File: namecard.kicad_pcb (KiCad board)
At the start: 2 copper layers, 85.6 x 54 mm, 29 parts, among them J1 Conn_01x24, J2 Conn_01x05, Q1 AO3400A, U1 STM32G030K6Tx, U2 ST25DV04K-IER8C3

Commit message: 基盤配置の調整
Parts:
- removed C_Tank1: 330uF, Capacitor_Tantalum_SMD:CP_EIA-3216-18_Kemet-A
- added C13: 0.1uF, Capacitor_SMD:C_0603_1608Metric, F.Cu at (152.5, 89.5)
- added C14: 22uf, Capacitor_SMD:C_0805_2012Metric, F.Cu at (111.5, 81.0)
- added C15: 22uf, Capacitor_SMD:C_0805_2012Metric, F.Cu at (111.5, 78.0)
- added C16: 22uf, Capacitor_SMD:C_0805_2012Metric, F.Cu at (111.5, 75.0)
- added C17: 22uf, Capacitor_SMD:C_0805_2012Metric, F.Cu at (115.5, 75.5)
- added C18: 22uf, Capacitor_SMD:C_0805_2012Metric, F.Cu at (118.5, 75.5)
- added C19: 22uf, Capacitor_SMD:C_0805_2012Metric, F.Cu at (121.5, 75.5)
- added C20: 22uf, Capacitor_SMD:C_0805_2012Metric, F.Cu at (124.5, 75.5)
- added C21: 22uf, Capacitor_SMD:C_0805_2012Metric, F.Cu at (121.5, 79.2)
- added C22: 22uf, Capacitor_SMD:C_0805_2012Metric, F.Cu at (118.5, 79.2)
- added C23: 22uf, Capacitor_SMD:C_0805_2012Metric, F.Cu at (115.5, 79.2)
- added C8: 0.1uF, Capacitor_SMD:C_0603_1608Metric, F.Cu at (129.0, 85.7)
- added D4: D_Schottky, Diode_SMD:D_SOD-123, F.Cu at (124.5, 80.0)
- moved C3 27.8 mm to (128.5, 92.5), turned to 180 degrees
- moved D2 27.4 mm to (133.0, 95.5)
- moved D1 27.2 mm to (133.0, 92.5)
- moved D3 21.0 mm to (121.7, 84.0), turned to 0 degrees
- moved C5 15.8 mm to (117.2, 84.0), turned to 0 degrees
- moved C4 12.5 mm to (124.0, 88.5)
- moved L1 12.5 mm to (119.5, 88.5)
- moved Q1 12.5 mm to (120.0, 92.6)
- moved R1 12.5 mm to (124.0, 94.5)
- moved R2 12.5 mm to (124.0, 91.5)
- moved J2 11.5 mm to (151.9, 84.5), turned to 90 degrees
- moved C6 7.23 mm to (153.5, 92.5), turned to 90 degrees
- moved C2 5.39 mm to (157.0, 98.5)
- moved C7 5.11 mm to (155.0, 92.5), turned to 90 degrees
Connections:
- net +3.3V renamed /EXT_3V3
- U2 pad 1: unconnected-(U2-V_EH-Pad1) -> /V_EH_RAW
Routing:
- net /V_EH_RAW: track 0.00 -> 39.4 mm
- net /PREVGL: track 64.1 -> 36.1 mm
- net /EXT_3V3: track 95.8 -> 69.2 mm, vias 3 -> 4
- net /GDR: track 66.0 -> 51.1 mm
- net /RESE: track 66.4 -> 51.7 mm
- net /PREVGH: track 68.8 -> 54.7 mm, vias 2 -> 4
- net /SWDIO: track 15.5 -> 9.75 mm
- net Net-(J1-Pin_15): track 11.8 -> 16.8 mm
- net Net-(D3-A): track 16.9 -> 21.8 mm
- net /EPD_CS: track 37.4 -> 32.7 mm
- net Net-(J1-Pin_18): track 6.07 -> 10.8 mm
- net GND: track 12.9 -> 9.01 mm
- net Net-(J1-Pin_5): track 5.94 -> 8.54 mm
- net /NRST: track 28.0 -> 30.1 mm, vias 1 -> 2
- net Net-(D1-K): track 8.06 -> 5.93 mm
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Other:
- board text added: "NRST"

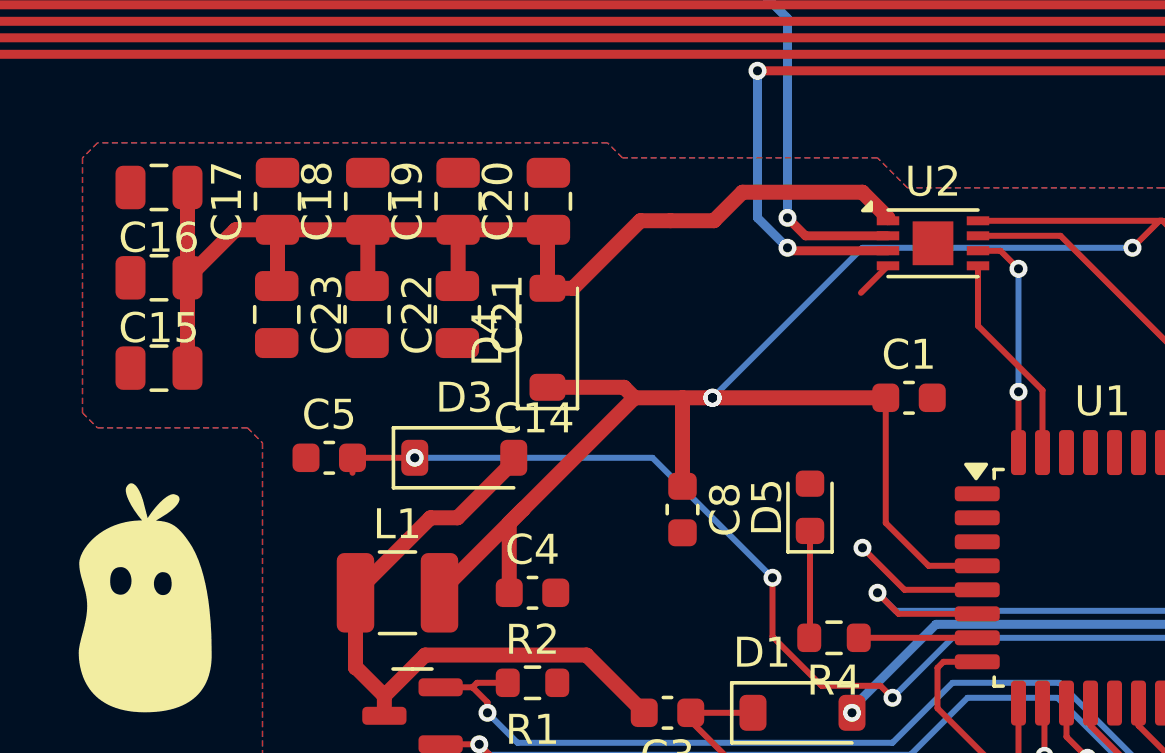
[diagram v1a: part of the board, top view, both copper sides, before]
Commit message: 電源の太さの調整
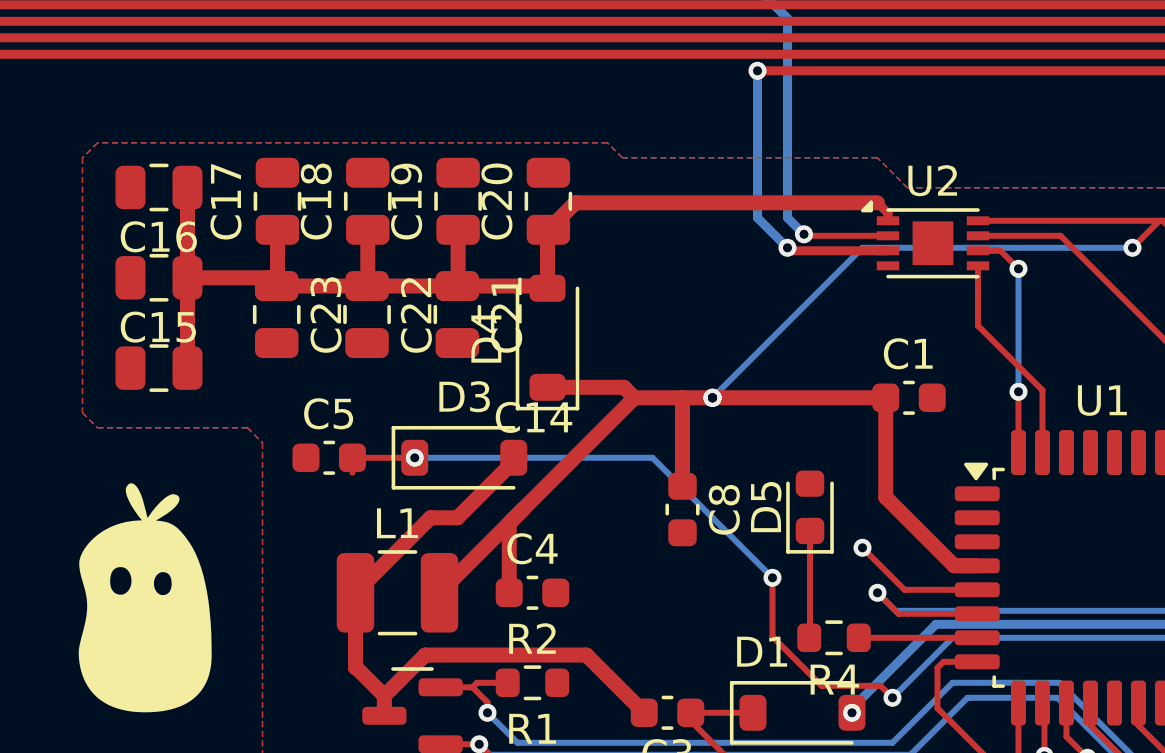
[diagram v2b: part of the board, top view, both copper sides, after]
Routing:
- net /V_EH_RAW: track 39.4 -> 37.9 mm
- net GND: track 9.01 -> 7.74 mm
- net /EXT_3V3: track 69.2 -> 68.7 mm

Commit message: v2 production
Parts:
- J1: footprint Connector_FFC-FPC:Hirose_FH12-24S-0.5SH_1x24-1MP_P0.50mm_Horizontal -> Connector:FFC-SMD_24P-P0.50_FH34SRJ-24S-0.5SH
- moved C1 18.8 mm to (122.5, 94.5), turned to 90 degrees
- moved D5 17.1 mm to (140.8, 101.0), turned to 0 degrees
- moved C22 16.8 mm to (131.7, 89.6)
- moved C21 16.8 mm to (134.7, 89.6)
- moved C23 16.8 mm to (128.7, 89.6)
- moved C17 14.8 mm to (126.0, 85.8)
- moved C18 14.8 mm to (129.0, 85.8)
- moved C19 14.8 mm to (132.0, 85.8)
- moved C20 14.8 mm to (135.0, 85.8)
- moved C16 14.6 mm to (122.0, 85.2)
- moved C15 14.5 mm to (122.0, 88.0)
- moved C14 14.3 mm to (122.0, 90.8)
- moved D4 14.0 mm to (125.2, 94.0)
- moved R4 11.5 mm to (137.5, 101.0), turned to 0 degrees
- moved C8 10.5 mm to (135.8, 93.8)
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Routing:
- net /EXT_3V3: track 68.7 -> 47.6 mm, vias 4 -> 2
- net Net-(U2-AC0): track 1244.1 -> 1264.7 mm
- net Net-(D3-A): track 21.8 -> 29.7 mm
- net /NFC_INT: track 20.7 -> 13.1 mm
- net Net-(J1-Pin_15): track 16.8 -> 23.4 mm
- net /PREVGH: track 54.7 -> 60.7 mm, vias 4 -> 2
- net /GDR: track 51.1 -> 57.0 mm
- net /RESE: track 51.7 -> 57.6 mm
- net GND: track 7.74 -> 13.3 mm, vias 3 -> 6
- net /SWDIO: track 9.75 -> 14.8 mm, vias 2 -> 1
- net /PREVGL: track 36.1 -> 40.6 mm
- net /SPI_SCK: track 25.1 -> 29.4 mm
- net /SPI_MOSI: track 23.3 -> 27.5 mm
- net Net-(U1-PA0): track 3.95 -> 7.57 mm
- net Net-(J1-Pin_22): track 8.61 -> 11.9 mm
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
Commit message: V3向けの変更:LEDの向きを直したり
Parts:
- turned D5 to 180 degrees
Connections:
- D5 pad 1: Net-(D5-K) -> GND
- D5 pad 2: GND -> Net-(D5-A)
- R4 pad 2: Net-(D5-K) -> Net-(D5-A)
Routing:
- net Net-(D5-K): track 1.64 -> 0.00 mm
- net Net-(D5-A): track 0.00 -> 1.64 mm
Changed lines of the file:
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@@
 		(0 "F.Cu" signal)
 		(2 "B.Cu" signal)
-		(9 "F.Adhes" user)
-		(11 "B.Adhes" user)
+		(9 "F.Adhes" user "F.Adhesive")
+		(11 "B.Adhes" user "B.Adhesive")
 		(13 "F.Paste" user)
 		(15 "B.Paste" user)
-		(5 "F.SilkS" user)
-		(7 "B.SilkS" user)
+		(5 "F.SilkS" user "F.Silkscreen")
+		(7 "B.SilkS" user "B.Silkscreen")
 		(1 "F.Mask" user)
 		(3 "B.Mask" user)
-		(17 "Dwgs.User" user)
-		(19 "Cmts.User" user)
-		(21 "Eco1.User" user)
-		(23 "Eco2.User" user)
+		(17 "Dwgs.User" user "User.Drawings")
+		(19 "Cmts.User" user "User.Comments")
+		(21 "Eco1.User" user "User.Eco1")
+		(23 "Eco2.User" user "User.Eco2")
 		(25 "Edge.Cuts" user)
 		(27 "Margin" user)
-		(31 "F.CrtYd" user)
-		(29 "B.CrtYd" user)
+		(31 "F.CrtYd" user "F.Courtyard")
+		(29 "B.CrtYd" user "B.Courtyard")
 		(35 "F.Fab" user)
 		(33 "B.Fab" user)
@@
 			)
 		)
+		(property "LCSC" "C45783"
+			(at 0 0 180)
+			(unlocked yes)
+			(layer "F.Fab")
+			(hide yes)
+			(effects
+				(font
+					(size 1 1)
+					(thickness 0.15)
+				)
+			)
+		)
 		(property ki_fp_filters "C_*")
 		(sheetname "/")
@@
 				(font
 					(size 1.27 1.27)
+					(thickness 0.15)
 				)
 			)
@@
 				(font
 					(size 1.27 1.27)
+					(thickness 0.15)
+				)
+			)
+		)
+		(property "LCSC" "C324726"
+			(at 0 0 90)
+			(unlocked yes)
+			(layer "F.Fab")
+			(hide yes)
+			(effects
+				(font
+					(size 1 1)
+					(thickness 0.15)
 				)
 			)
@@
 	(footprint "LED_SMD:LED_0603_1608Metric"
 		(layer "F.Cu")
-		(at 140.75 101)
+		(at 140.75 101 180)
 		(descr "LED SMD 0603 (1608 Metric), square (rectangular) end terminal, IPC-7351 nominal, (Body size source: http://www.tortai-tech.com/upload/download/2011102023233369053.pdf)")
 		(tags "LED")
@@
 		)
 		(property "KiLib_Generator" "1=K 2=A"
-			(at 0 0 0)
+			(at 0 0 180)
 			(unlocked yes)
 			(layer "F.Fab")
@@
 		)
 		(property "Sim.Pins" "1=K 2=A"
-			(at 0 0 0)
+			(at 0 0 180)
 			(unlocked yes)
 			(layer "F.Fab")
@@
 		(duplicate_pad_numbers_are_jumpers no)
 		(fp_line
-			(start -1.485 -0.735)
-			(end -1.485 0.735)
+			(start 0.8 -0.735)
+			(end -1.485 -0.735)
 			(stroke
 				(width 0.12)
@@
 		)
 		(fp_line
-			(start 0.8 -0.735)
-			(end -1.485 -0.735)
+			(start -1.485 -0.735)
+			(end -1.485 0.735)
 			(stroke
 				(width 0.12)
@@
 		)
 		(fp_line
-			(start -0.8 -0.1)
-			(end -0.8 0.4)
+			(start 0.8 0.4)
+			(end 0.8 -0.4)
 			(stroke
 				(width 0.1)
@@
 		)
 		(fp_line
-			(start -0.8 0.4)
-			(end 0.8 0.4)
+			(start 0.8 -0.4)
+			(end -0.5 -0.4)
 			(stroke
 				(width 0.1)
@@
 		)
 		(fp_line
-			(start 0.8 -0.4)
-			(end -0.5 -0.4)
+			(start -0.8 0.4)
+			(end 0.8 0.4)
 			(stroke
 				(width 0.1)
@@
 		)
 		(fp_line
-			(start 0.8 0.4)
-			(end 0.8 -0.4)
+			(start -0.8 -0.1)
+			(end -0.8 0.4)
 			(stroke
 				(width 0.1)
@@
 		)
 		(pad "1" smd roundrect
-			(at -0.7875 0)
+			(at -0.7875 0 180)
 			(size 0.875 0.95)
 			(layers "F.Cu" "F.Mask" "F.Paste")
 			(roundrect_rratio 0.25)
-			(net "Net-(D5-K)")
+			(net "GND")
 			(pinfunction "K_1")
 			(pintype "passive")
 		)
 		(pad "2" smd roundrect
-			(at 0.7875 0)
+			(at 0.7875 0 180)
 			(size 0.875 0.95)
 			(layers "F.Cu" "F.Mask" "F.Paste")
 			(roundrect_rratio 0.25)
-			(net "GND")
+			(net "Net-(D5-A)")
 			(pinfunction "A_2")
 			(pintype "passive")
@@
 			)
 		)
+		(property "LCSC" "C45783"
+			(at 0 0 90)
+			(unlocked yes)
+			(layer "F.Fab")
+			(hide yes)
+			(effects
+				(font
+					(size 1 1)
+					(thickness 0.15)
+				)
+			)
+		)
 		(property ki_fp_filters "C_*")
 		(sheetname "/")
@@
 			)
 		)
+		(property "LCSC" "C45783"
+			(at 0 0 270)
+			(unlocked yes)
+			(layer "F.Fab")
+			(hide yes)
+			(effects
+				(font
+					(size 1 1)
+					(thickness 0.15)
+				)
+			)
+		)
 		(property ki_fp_filters "C_*")
 		(sheetname "/")
@@
 			(layers "F.Cu" "F.Mask" "F.Paste")
 			(roundrect_rratio 0.25)
-			(net "Net-(D5-K)")
+			(net "Net-(D5-A)")
 			(pintype "passive")
 		)
@@
 			)
 		)
+		(property "LCSC" "C2908287"
+			(at 0 0 0)
+			(unlocked yes)
+			(layer "F.Fab")
+			(hide yes)
+			(effects
+				(font
+					(size 1 1)
+					(thickness 0.15)
+				)
+			)
+		)
 		(property ki_fp_filters "DFN*3x2mm*P0.5mm*")
 		(sheetname "/")
@@
 			)
 		)
+		(property "LCSC" "C529331"
+			(at 0 0 0)
+			(unlocked yes)
+			(layer "F.Fab")
+			(hide yes)
+			(effects
+				(font
+					(size 1 1)
+					(thickness 0.15)
+				)
+			)
+		)
 		(property ki_fp_filters "LQFP*7x7mm*P0.8mm*")
 		(sheetname "/")
@@
 			)
 		)
+		(property "LCSC" "C22374920"
+			(at 0 0 90)
+			(unlocked yes)
+			(layer "F.Fab")
+			(hide yes)
+			(effects
+				(font
+					(size 1 1)
+					(thickness 0.15)
+				)
+			)
+		)
 		(property ki_fp_filters "TO-???* *_Diode_* *SingleDiode* D_*")
 		(sheetname "/")
@@
 			)
 		)
+		(property "LCSC" "C45783"
+			(at 0 0 90)
+			(unlocked yes)
+			(layer "F.Fab")
+			(hide yes)
+			(effects
+				(font
+					(size 1 1)
+					(thickness 0.15)
+				)
+			)
+		)
 		(property ki_fp_filters "C_*")
 		(sheetname "/")
@@
 			)
 		)
+		(property "LCSC" "C66936"
+			(at 0 0 0)
+			(unlocked yes)
+			(layer "F.Fab")
+			(hide yes)
+			(effects
+				(font
+					(size 1 1)
+					(thickness 0.15)
+				)
+			)
+		)
 		(property ki_fp_filters "Choke_* *Coil* Inductor_* L_*")
 		(sheetname "/")
@@
 			)
 		)
+		(property "LCSC" "C45783"
+			(at 0 0 180)
+			(unlocked yes)
+			(layer "F.Fab")
+			(hide yes)
+			(effects
+				(font
+					(size 1 1)
+					(thickness 0.15)
+				)
+			)
+		)
 		(property ki_fp_filters "C_*")
 		(sheetname "/")
@@
 			)
 		)
+		(property "LCSC" "C45783"
+			(at 0 0 90)
+			(unlocked yes)
+			(layer "F.Fab")
+			(hide yes)
+			(effects
+				(font
+					(size 1 1)
+					(thickness 0.15)
+				)
+			)
+		)
 		(property ki_fp_filters "C_*")
 		(sheetname "/")
@@
 			)
 		)
+		(property "LCSC" "C45783"
+			(at 0 0 270)
+			(unlocked yes)
+			(layer "F.Fab")
+			(hide yes)
+			(effects
+				(font
+					(size 1 1)
+					(thickness 0.15)
+				)
+			)
+		)
 		(property ki_fp_filters "C_*")
 		(sheetname "/")
@@
 			)
 		)
+		(property "LCSC" "C45783"
+			(at 0 0 90)
+			(unlocked yes)
+			(layer "F.Fab")
+			(hide yes)
+			(effects
+				(font
+					(size 1 1)
+					(thickness 0.15)
+				)
+			)
+		)
 		(property ki_fp_filters "C_*")
 		(sheetname "/")
@@
 			)
 		)
+		(property "LCSC" "C45783"
+			(at 0 0 270)
+			(unlocked yes)
+			(layer "F.Fab")
+			(hide yes)
+			(effects
+				(font
+					(size 1 1)
+					(thickness 0.15)
+				)
+			)
+		)
 		(property ki_fp_filters "C_*")
 		(sheetname "/")
@@
 			)
 		)
+		(property "LCSC" "C45783"
+			(at 0 0 180)
+			(unlocked yes)
+			(layer "F.Fab")
+			(hide yes)
+			(effects
+				(font
+					(size 1 1)
+					(thickness 0.15)
+				)
+			)
+		)
 		(property ki_fp_filters "C_*")
 		(sheetname "/")
@@
 	)
 	(segment
-		(start 138.325 101)
-		(end 139.9625 101)
-		(width 0.2)
-		(layer "F.Cu")
-		(net "Net-(D5-K)")
-	)
-	(segment
 		(start 129.275 97)
 		(end 131.35 97)
@@
 		(net "/NFC_INT")
 	)
+	(segment
+		(start 138.325 101)
+		(end 139.9625 101)
+		(width 0.2)
+		(layer "F.Cu")
+		(net "Net-(D5-A)")
+	)
 	(zone

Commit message: v3
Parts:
- removed C19, C20, C21, C22: 22uf, Capacitor_SMD:C_0805_2012Metric
- removed D5: LED, LED_SMD:LED_0603_1608Metric
- removed REF** (x4): MountingHole_2.2mm_M2, MountingHole:MountingHole_2.2mm_M2
- added R3: 1M, Resistor_SMD:R_0603_1608Metric, F.Cu at (133.0, 94.5)
- added R5: 470k, Resistor_SMD:R_0603_1608Metric, F.Cu at (137.5, 99.0)
- added TP1: TestPoint, TestPoint:TestPoint_Pad_D1.0mm, F.Cu at (128.0, 90.5)
- added TP3: TestPoint, TestPoint:TestPoint_Pad_D1.0mm, F.Cu at (138.0, 88.0)
- added TP4: TestPoint, TestPoint:TestPoint_Pad_D1.0mm, F.Cu at (165.5, 87.5)
- added TP5: TestPoint, TestPoint:TestPoint_Pad_D1.0mm, F.Cu at (165.5, 84.0)
- added TP6: TestPoint, TestPoint:TestPoint_Pad_D1.0mm, F.Cu at (162.5, 90.5)
- added TP7: TestPoint, TestPoint:TestPoint_Pad_D1.0mm, F.Cu at (126.5, 94.0)
- added U3: TPS22917DBV, Package_TO_SOT_SMD:SOT-23-6, F.Cu at (156.0, 88.0)
- C14, C15, C16, C17: value 22uf -> 220uf; footprint Capacitor_SMD:C_0805_2012Metric -> Capacitor_Tantalum_SMD:6TPE220MAZB
- C18: value 22uf -> 100nf; footprint Capacitor_SMD:C_0805_2012Metric -> Capacitor_SMD:C_0603_1608Metric
- D4: footprint Diode_SMD:D_SOD-123 -> Diode_SMD:D_SOD-123F
- J1: footprint Connector:FFC-SMD_24P-P0.50_FH34SRJ-24S-0.5SH -> Connector_FFC-FPC:Hirose_FH12-24S-0.5SH_1x24-1MP_P0.50mm_Horizontal
- R4: value 1K -> 100k
- moved C18 27.6 mm to (156.0, 91.5), turned to 0 degrees
- moved R4 25.5 mm to (160.0, 89.0)
- moved C5 16.3 mm to (125.0, 99.5), turned to -90 degrees
- moved C12 15.7 mm to (153.0, 101.0), turned to 0 degrees
- moved D3 13.5 mm to (121.5, 100.5), turned to 180 degrees
- moved C11 11.3 mm to (157.0, 99.5), turned to 180 degrees
- moved C10 10.7 mm to (153.0, 98.0), turned to 180 degrees
- moved C2 10.3 mm to (153.0, 91.5)
- moved C16 9.58 mm to (131.5, 86.5), turned to 90 degrees
- moved D4 9.28 mm to (133.8, 90.5), turned to 0 degrees
- moved C1 8.38 mm to (130.5, 92.0)
- moved C23 6.63 mm to (135.0, 87.5), turned to 90 degrees
- moved C13 5.30 mm to (150.0, 88.0), turned to 90 degrees
- moved C9 5.02 mm to (157.0, 93.5), turned to 180 degrees
- moved C7 4.47 mm to (157.0, 96.5), turned to 180 degrees
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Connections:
- C10 pad 1: Net-(J1-Pin_22) -> Net-(J1-Pin_3)
- C11 pad 1: GND -> /PREVGL
- C11 pad 2: /PREVGL -> GND
- C12 pad 2: Net-(J1-Pin_24) -> Net-(J1-Pin_1)
- C14 pad 1: /V_EH_RAW -> /EXT_3V3
- C15 pad 1: /V_EH_RAW -> /EXT_3V3
- C16 pad 1: /V_EH_RAW -> /EXT_3V3
- C17 pad 1: /V_EH_RAW -> /EXT_3V3
- C18 pad 1: /V_EH_RAW -> GND
- C18 pad 2: GND -> /EPD_SW
- C2 pad 1: Net-(J1-Pin_5) -> Net-(J1-Pin_17)
- C6 pad 1: Net-(J1-Pin_15) -> Net-(J1-Pin_7)
- C7 pad 1: Net-(J1-Pin_18) -> Net-(J1-Pin_5)
- C9 pad 1: Net-(J1-Pin_20) -> /EPD_SW
- J1 pad 1: unconnected-(J1-Pin_1-Pad1) -> Net-(J1-Pin_1)
- J1 pad 10: /EPD_RST -> /EPD_SW
- J1 pad 11: /EPD_DC -> /SPI_MOSI
- J1 pad 12: /EPD_CS -> /SPI_SCK
- J1 pad 13: /SPI_SCK -> /EPD_CS
- J1 pad 14: /SPI_MOSI -> /EPD_DC
- J1 pad 15: Net-(J1-Pin_15) -> /EPD_RST
- J1 pad 16: Net-(J1-Pin_15) -> /EPD_BUSY
- J1 pad 17: GND -> Net-(J1-Pin_17)
- J1 pad 18: Net-(J1-Pin_18) -> unconnected-(J1-Pin_18-Pad18)
- J1 pad 2: /GDR -> /PREVGL
- J1 pad 20: Net-(J1-Pin_20) -> GND
- J1 pad 21: /PREVGH -> unconnected-(J1-Pin_21-Pad21)
- J1 pad 22: Net-(J1-Pin_22) -> /RESE
- J1 pad 23: /PREVGL -> /GDR
- J1 pad 24: Net-(J1-Pin_24) -> unconnected-(J1-Pin_24-Pad24)
- J1 pad 3: /RESE -> Net-(J1-Pin_3)
- J1 pad 4: unconnected-(J1-Pin_4-Pad4) -> /PREVGH
- J1 pad 7: unconnected-(J1-Pin_7-Pad7) -> Net-(J1-Pin_7)
- J1 pad 9: /EPD_BUSY -> /EPD_SW
- R4 pad 1: Net-(U1-PA0) -> Net-(U3-CT)
- R4 pad 2: Net-(D5-A) -> GND
- U1 pad 13: unconnected-(U1-PA6-Pad13) -> Net-(U1-PA6)
- U1 pad 22: unconnected-(U1-PA9/PA11-Pad22) -> Net-(U1-PA9/PA11)
- U1 pad 23: unconnected-(U1-PA10/PA12-Pad23) -> Net-(U1-PA10/PA12)
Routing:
- net /EXT_3V3: track 47.6 -> 78.1 mm
- net /V_EH_RAW: track 40.2 -> 13.1 mm
- net /EPD_SW: track 0.00 -> 23.9 mm, vias 0 -> 3
- net Net-(J1-Pin_15): track 23.4 -> 0.00 mm
- net Net-(U1-PA10/PA12): track 0.00 -> 21.2 mm, vias 0 -> 2
- net Net-(U1-PA9/PA11): track 0.00 -> 20.1 mm, vias 0 -> 2
- net Net-(U1-PA6): track 0.00 -> 19.0 mm, vias 0 -> 2
- net /PREVGH: track 60.7 -> 44.4 mm
- net Net-(J1-Pin_7): track 0.00 -> 15.3 mm, vias 0 -> 2
- net Net-(J1-Pin_20): track 14.6 -> 0.00 mm
- net Net-(J1-Pin_17): track 0.00 -> 14.2 mm
- net Net-(J1-Pin_18): track 14.1 -> 0.00 mm
- net Net-(J1-Pin_3): track 0.00 -> 13.3 mm
- net Net-(J1-Pin_1): track 0.00 -> 12.5 mm
- net GND: track 13.3 -> 25.6 mm, vias 6 -> 12
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
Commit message: wip: 電源周りの回路図を更新
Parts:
- added C19: 1nf, Capacitor_SMD:C_0603_1608Metric, F.Cu at (116.0, 75.3)
- added R6: 10k, Resistor_SMD:R_0603_1608Metric, F.Cu at (116.0, 80.3)
- R4: value 100k -> 10k
- moved R4 45.4 mm to (116.0, 77.8)
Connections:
- C4 pad 1: /EXT_3V3 -> /EPD_SW
- L1 pad 2: /EXT_3V3 -> /EPD_SW
- R4 pad 1: Net-(U3-CT) -> /I2C_SDA
- R4 pad 2: GND -> /EXT_3V3
- U3 pad 2: unconnected-(U3-GND-Pad2) -> GND
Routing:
- net Net-(U3-CT): vias 3 -> 2
- net /EPD_SW: vias 3 -> 2

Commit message: wip: v3向けに配置を更新
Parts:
- removed C18: 100nf, Capacitor_SMD:C_0603_1608Metric
- removed C9: 1uF, Capacitor_SMD:C_0603_1608Metric
- moved TP6 49.2 mm to (113.5, 87.0)
- moved U3 38.1 mm to (118.0, 90.0), turned to 90 degrees
- moved R4 29.0 mm to (143.5, 87.0)
- moved R6 28.0 mm to (143.5, 85.5)
- moved TP5 13.3 mm to (153.0, 88.5)
- moved C19 11.9 mm to (118.0, 87.0), turned to 180 degrees
- moved TP4 10.0 mm to (155.5, 88.5)
- moved C2 4.72 mm to (157.0, 94.0)
- moved U2 2.38 mm to (143.5, 83.0)
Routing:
- net /EPD_SW: track 23.9 -> 69.4 mm, vias 2 -> 5
- net /GDR: track 56.3 -> 89.8 mm
- net Net-(U1-PA10/PA12): track 21.2 -> 6.86 mm
- net Net-(U1-PA6): track 19.0 -> 30.6 mm
- net Net-(U1-PA9/PA11): track 20.1 -> 9.69 mm
- net Net-(J1-Pin_17): track 14.2 -> 8.09 mm
- net GND: track 25.6 -> 19.8 mm, vias 12 -> 11
- net /SWCLK: track 17.6 -> 13.1 mm
- net /SWDIO: track 14.8 -> 10.5 mm
- net Net-(U2-AC0): track 1264.7 -> 1261.6 mm
- net /NFC_INT: track 13.1 -> 16.0 mm, vias 0 -> 2
- net /V_EH_RAW: track 13.1 -> 16.0 mm
- net /I2C_SDA: track 5.94 -> 8.54 mm
- net /EXT_3V3: track 78.1 -> 75.5 mm
- net /RESE: track 57.1 -> 56.1 mm
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
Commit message: wip: 配置を更新
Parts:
- added C18: 100nf, Capacitor_SMD:C_0603_1608Metric, F.Cu at (153.5, 88.5)
- added C9: 1uF, Capacitor_SMD:C_0603_1608Metric, F.Cu at (153.5, 90.0)
- moved TP5 7.07 mm to (160.0, 87.5)
- moved TP4 4.74 mm to (160.0, 90.0)
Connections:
- net /EXT_3V3 renamed /SYS_VDD
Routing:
- net /GDR: track 89.8 -> 58.4 mm
- net Net-(U1-PA10/PA12): track 6.86 -> 14.3 mm
- net Net-(U1-PA9/PA11): track 9.69 -> 13.6 mm
- net /EPD_SW: track 69.4 -> 72.5 mm, vias 5 -> 4
- net /SYS_VDD: track 75.5 -> 77.4 mm
- net /RESE: track 56.1 -> 57.3 mm
